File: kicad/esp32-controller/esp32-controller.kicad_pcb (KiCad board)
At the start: 2 copper layers, 74.9 x 89.9 mm, 47 parts, among them J1 RJ45, J2 RJ45, J3 RJ45, J4 RJ45, J5 RJ45, J6 RJ45, J7 Barrel_Jack_Switch, J8 Conn_01x04_Pin, U1 SN65LVDS049, U10 74AHC1G08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

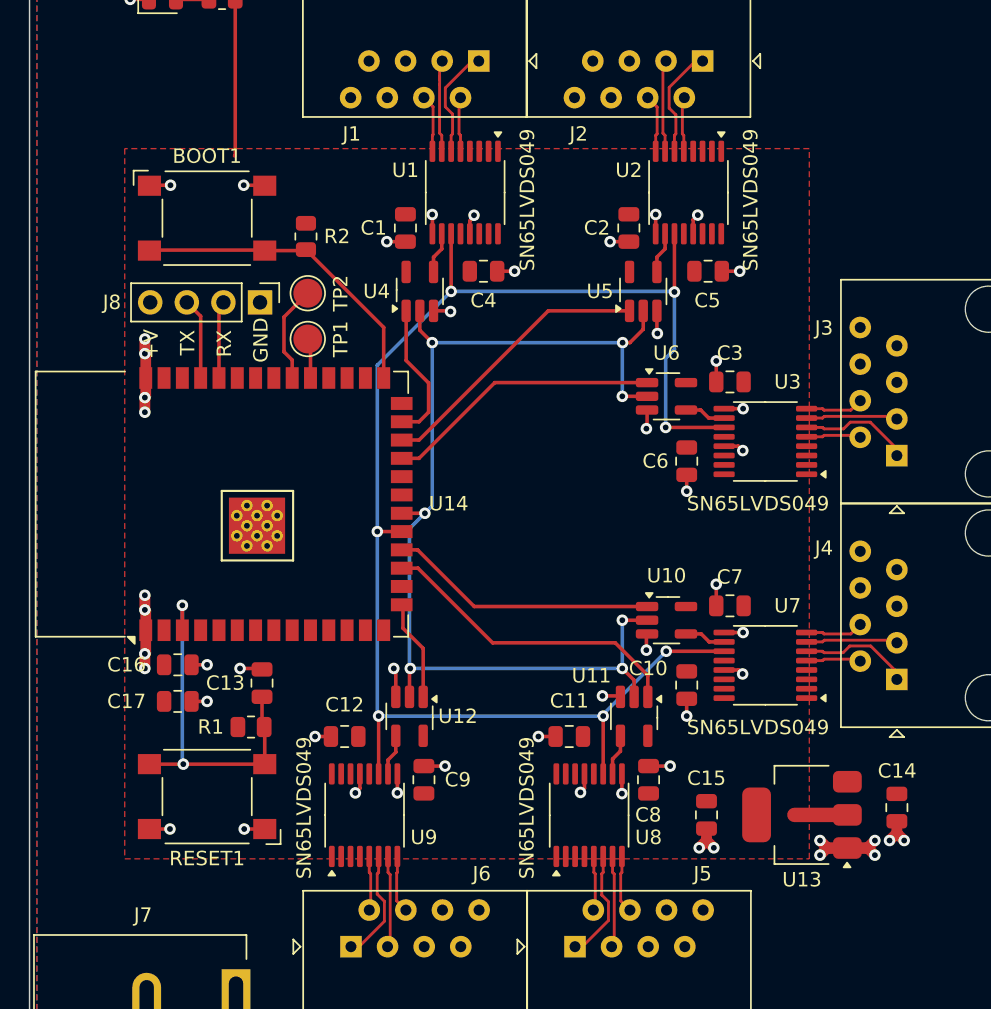
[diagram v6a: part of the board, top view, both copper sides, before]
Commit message: Add testpoints to pcbs
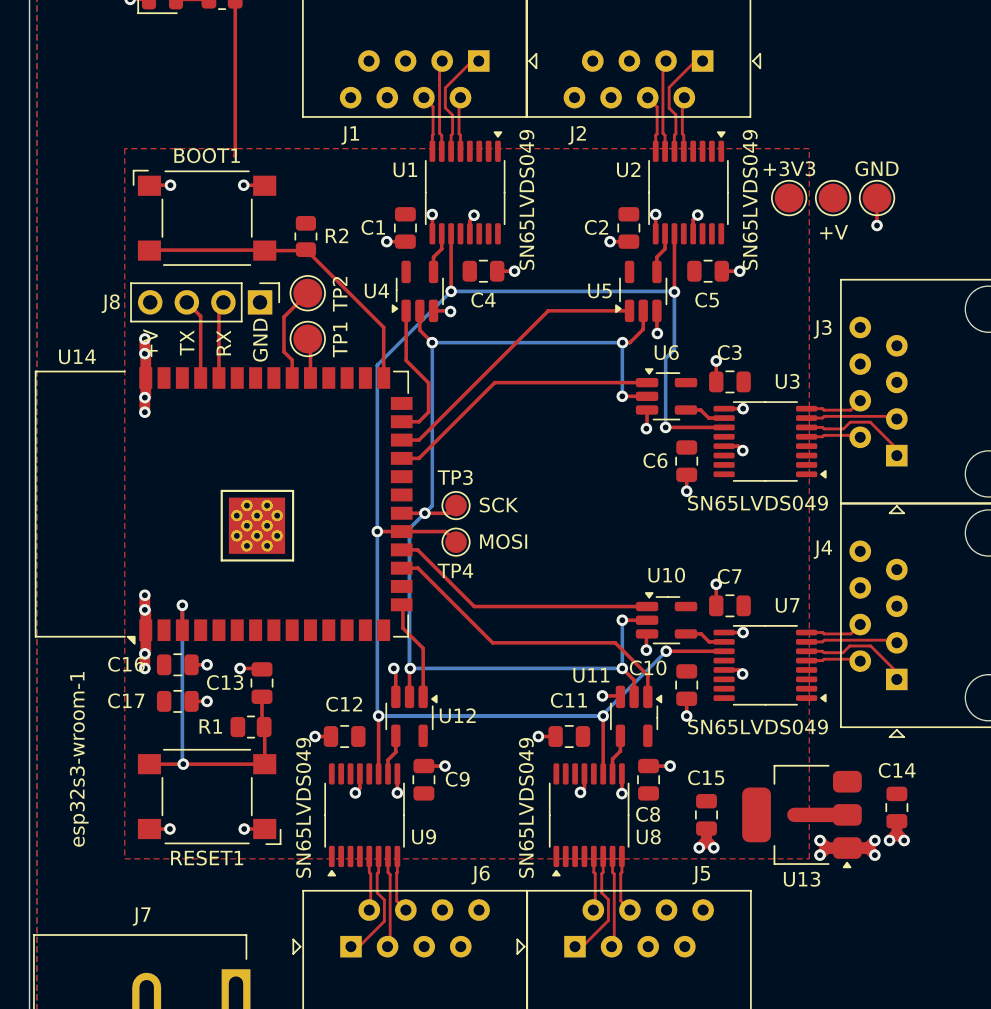
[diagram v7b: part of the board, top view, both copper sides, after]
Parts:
- added +3V3: TestPoint_Pad_D2.0mm, TestPoint:TestPoint_Pad_D2.0mm, F.Cu at (164.7, 80.1)
- added +V: TestPoint_Pad_D2.0mm, TestPoint:TestPoint_Pad_D2.0mm, F.Cu at (167.8, 80.1)
- added GND: TestPoint_Pad_D2.0mm, TestPoint:TestPoint_Pad_D2.0mm, F.Cu at (170.8, 80.1)
- added TP3: SCK, TestPoint:TestPoint_Pad_D1.5mm, F.Cu at (141.6, 101.5)
- added TP4: MOSI, TestPoint:TestPoint_Pad_D1.5mm, F.Cu at (141.6, 104.0)
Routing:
- net /MOSI: track 104.6 -> 108.7 mm
- net /SCK: track 73.3 -> 75.7 mm
- net GND: track 74.7 -> 76.6 mm, vias 54 -> 55
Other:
- board text added: "esp32s3-wroom-1"
